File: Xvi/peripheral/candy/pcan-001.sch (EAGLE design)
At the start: 21 parts

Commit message: Optocoupler.
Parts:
- added JP1: Optorelay, pinhead:PINHD-1X2
- added OK1: LTV816, optocoupler:LTV816
- added R1: 220, rcl:R-EU_0204/5
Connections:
- new net N$17: OK1.A, R1.2
- new net N$19: JP1.2, OK1.EMIT
- new net N$20: JP1.1, OK1.COL
- net GND: now also OK1.C
- net MNTR: now also R1.1
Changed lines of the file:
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@@
 <part name="RN1" library="resistor-dil" library_urn="urn:adsk.eagle:library:342" deviceset="8R-N" device="" package3d_urn="urn:adsk.eagle:package:922/2" value="330"/>
 <part name="RN2" library="resistor-dil" library_urn="urn:adsk.eagle:library:342" deviceset="8R-N" device="" package3d_urn="urn:adsk.eagle:package:922/2" value="330"/>
+<part name="OK1" library="optocoupler" library_urn="urn:adsk.eagle:library:320" deviceset="LTV816" device="" package3d_urn="urn:adsk.eagle:package:21938/1"/>
+<part name="R1" library="rcl" library_urn="urn:adsk.eagle:library:334" deviceset="R-EU_" device="0204/5" package3d_urn="urn:adsk.eagle:package:23488/1" value="220"/>
+<part name="SUPPLY2" library="supply2" library_urn="urn:adsk.eagle:library:372" deviceset="GND" device=""/>
+<part name="JP1" library="pinhead" library_urn="urn:adsk.eagle:library:325" deviceset="PINHD-1X2" device="" package3d_urn="urn:adsk.eagle:package:22435/2" value="Optorelay"/>
 </parts>
 <sheets>
@@
 <attribute name="VALUE" x="55.88" y="17.272" size="1.778" layer="96"/>
 <attribute name="NAME" x="48.26" y="17.272" size="1.778" layer="95"/>
+</instance>
+<instance part="OK1" gate="G$1" x="121.92" y="226.06" smashed="yes">
+<attribute name="NAME" x="114.935" y="231.775" size="1.778" layer="95"/>
+<attribute name="VALUE" x="114.935" y="218.44" size="1.778" layer="96"/>
+</instance>
+<instance part="R1" gate="G$1" x="104.14" y="228.6" smashed="yes">
+<attribute name="NAME" x="100.33" y="230.0986" size="1.778" layer="95"/>
+<attribute name="VALUE" x="100.33" y="225.298" size="1.778" layer="96"/>
+</instance>
+<instance part="SUPPLY2" gate="GND" x="109.22" y="218.44" smashed="yes">
+<attribute name="VALUE" x="107.315" y="215.265" size="1.778" layer="96"/>
+</instance>
+<instance part="JP1" gate="G$1" x="144.78" y="223.52" smashed="yes">
+<attribute name="NAME" x="138.43" y="229.235" size="1.778" layer="95"/>
+<attribute name="VALUE" x="138.43" y="218.44" size="1.778" layer="96"/>
 </instance>
 </instances>
@@
 <label x="231.14" y="193.04" size="0.8128" layer="95" xref="yes"/>
 </segment>
+<segment>
+<pinref part="R1" gate="G$1" pin="1"/>
+<wire x1="99.06" y1="228.6" x2="96.52" y2="228.6" width="0.1524" layer="91"/>
+<label x="96.52" y="228.6" size="0.8128" layer="95" rot="R180" xref="yes"/>
+</segment>
 </net>
 <net name="GND" class="1">
@@
 <wire x1="200.66" y1="193.04" x2="200.66" y2="190.5" width="0.1524" layer="91"/>
 <pinref part="SUPPLY1" gate="GND" pin="GND"/>
+</segment>
+<segment>
+<pinref part="OK1" gate="G$1" pin="C"/>
+<wire x1="111.76" y1="223.52" x2="109.22" y2="223.52" width="0.1524" layer="91"/>
+<wire x1="109.22" y1="223.52" x2="109.22" y2="220.98" width="0.1524" layer="91"/>
+<pinref part="SUPPLY2" gate="GND" pin="GND"/>
+</segment>
+</net>
+<net name="N$17" class="0">
+<segment>
+<pinref part="OK1" gate="G$1" pin="A"/>
+<wire x1="111.76" y1="228.6" x2="109.22" y2="228.6" width="0.1524" layer="91"/>
+<pinref part="R1" gate="G$1" pin="2"/>
+</segment>
+</net>
+<net name="N$19" class="0">
+<segment>
+<pinref part="OK1" gate="G$1" pin="EMIT"/>
+<pinref part="JP1" gate="G$1" pin="2"/>
+<wire x1="129.54" y1="223.52" x2="142.24" y2="223.52" width="0.1524" layer="91"/>
+</segment>
+</net>
+<net name="N$20" class="0">
+<segment>
+<pinref part="OK1" gate="G$1" pin="COL"/>
+<wire x1="129.54" y1="228.6" x2="132.08" y2="228.6" width="0.1524" layer="91"/>
+<wire x1="132.08" y1="228.6" x2="132.08" y2="226.06" width="0.1524" layer="91"/>
+<pinref part="JP1" gate="G$1" pin="1"/>
+<wire x1="132.08" y1="226.06" x2="142.24" y2="226.06" width="0.1524" layer="91"/>
 </segment>
 </net>
@@
 packages will not be understood (or retained) with this version.
 </note>
+<note version="8.4" severity="warning">
+Since Version 8.4, EAGLE supports properties for SPICE simulation.
+Probes in schematics and SPICE mapping objects found in parts and library devices
+will not be understood with this version. Update EAGLE to the latest version
+for full support of SPICE simulation.
+</note>
 </compatibility>

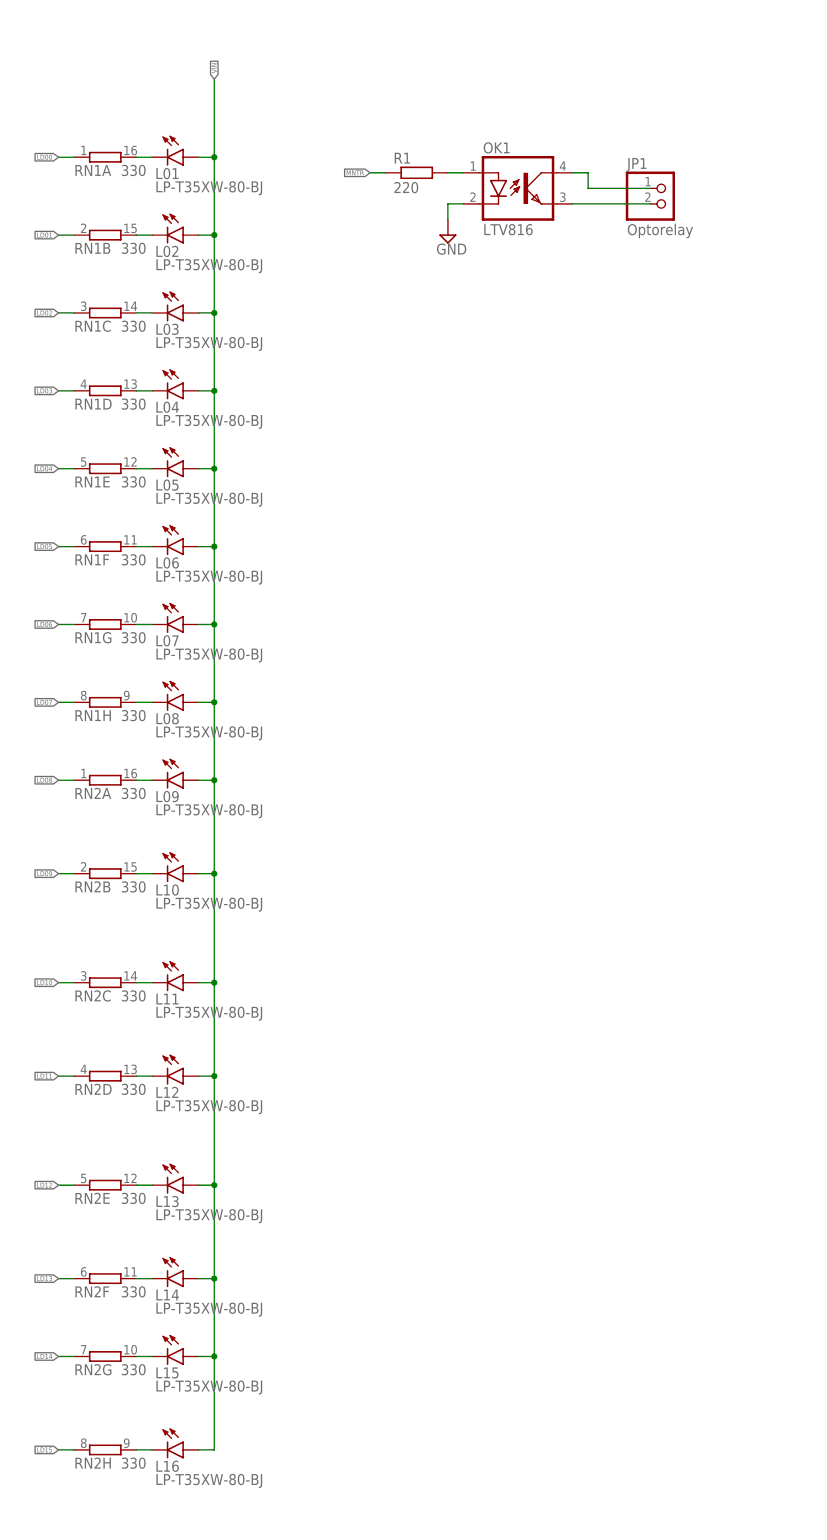
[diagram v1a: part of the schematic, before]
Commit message: Dual LEDs.
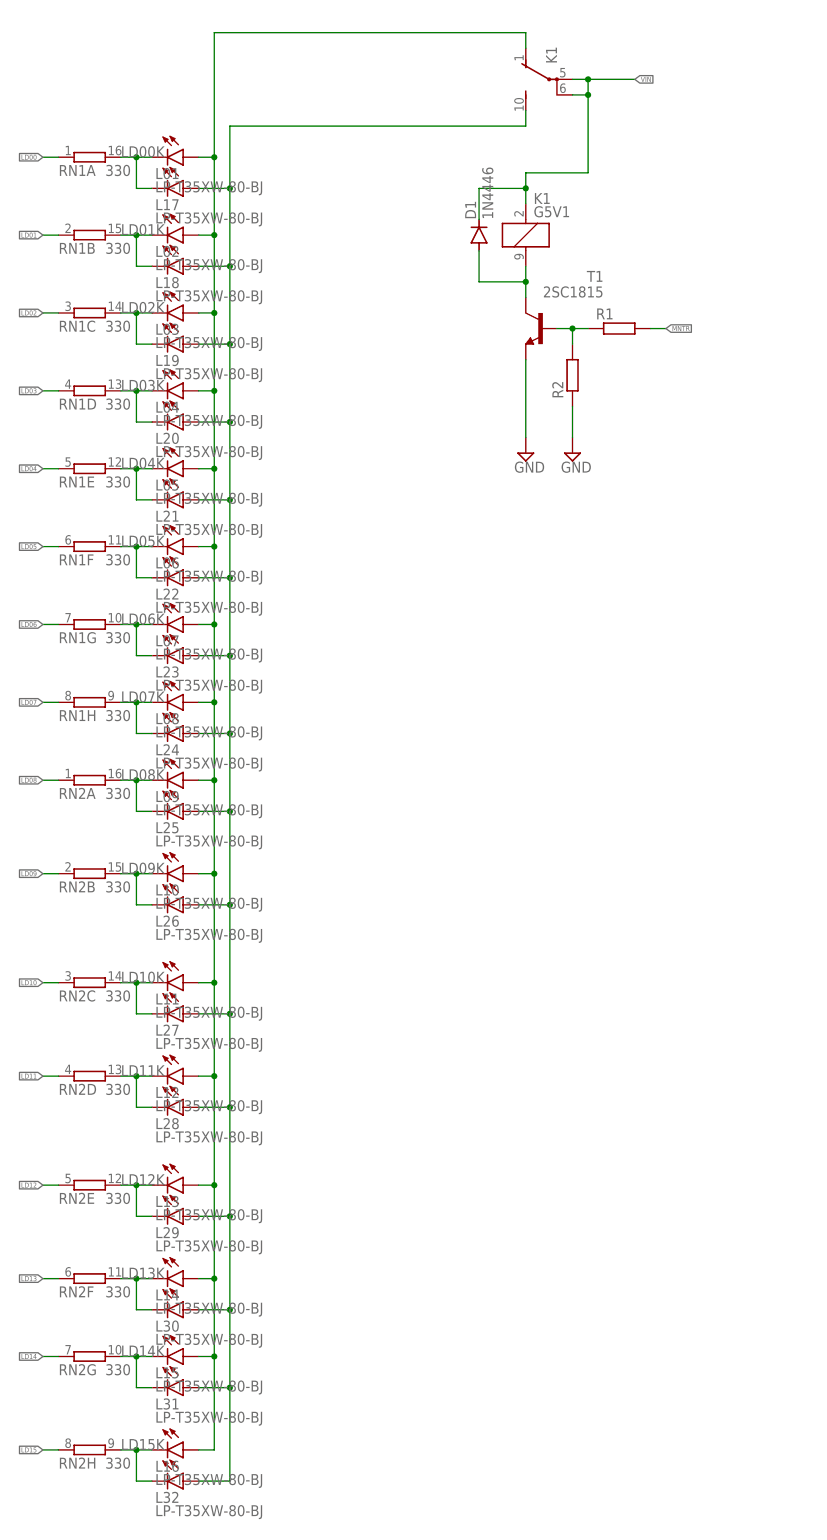
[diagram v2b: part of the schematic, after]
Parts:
- removed JP1: Optorelay, pinhead:PINHD-1X2
- removed OK1: LTV816, optocoupler:LTV816
- added D1: 1N4446, diode:1N4446
- added K1: G5V1, relay:G5V1
- added L17, L18, L19, L20, L21, L22, L23, L24, L25, L26, L27, L28, L29, L30, L31, L32: LP-T35XW-80-BJ, led:LEDKA-3528ASYC
- added R2: (no value), rcl:R-EU_0204/5
- added T1: 2SC1815, transistor:2SC1815
- R1: value 220 -> (none)
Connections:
- removed net N$1: L01.C, RN1A.2
- removed net N$10: L10.C, RN2B.2
- removed net N$11: L11.C, RN2C.2
- removed net N$12: L12.C, RN2D.2
- removed net N$13: L13.C, RN2E.2
- removed net N$14: L14.C, RN2F.2
- removed net N$15: L15.C, RN2G.2
- removed net N$16: L16.C, RN2H.2
- removed net N$2: L02.C, RN1B.2
- removed net N$20: JP1.1, OK1.COL
- removed net N$3: L03.C, RN1C.2
- removed net N$4: L04.C, RN1D.2
- removed net N$5: L05.C, RN1E.2
- removed net N$6: L06.C, RN1F.2
- removed net N$7: L07.C, RN1G.2
- removed net N$8: L08.C, RN1H.2
- removed net N$9: L09.C, RN2A.2
- new net LD00K: L01.C, L17.C, RN1A.2
- new net LD01K: L02.C, L18.C, RN1B.2
- new net LD02K: L03.C, L19.C, RN1C.2
- new net LD03K: L04.C, L20.C, RN1D.2
- new net LD04K: L05.C, L21.C, RN1E.2
- new net LD05K: L06.C, L22.C, RN1F.2
- new net LD06K: L07.C, L23.C, RN1G.2
- new net LD07K: L08.C, L24.C, RN1H.2
- new net LD08K: L09.C, L25.C, RN2A.2
- new net LD09K: L10.C, L26.C, RN2B.2
- new net LD10K: L11.C, L27.C, RN2C.2
- new net LD11K: L12.C, L28.C, RN2D.2
- new net LD12K: L13.C, L29.C, RN2E.2
- new net LD13K: L14.C, L30.C, RN2F.2
- new net LD14K: L15.C, L31.C, RN2G.2
- new net LD15K: L16.C, L32.C, RN2H.2
- new net VINA: K12.O, L01.A, L02.A, L03.A, L04.A, L05.A, L06.A, L07.A, L08.A, L09.A, L10.A, L11.A, L12.A, L13.A, L14.A, L15.A, L16.A
- new net VINB: K12.S, L17.A, L18.A, L19.A, L20.A, L21.A, L22.A, L23.A, L24.A, L25.A, L26.A, L27.A, L28.A, L29.A, L30.A, L31.A, L32.A
- net GND: now also R2.1, T1.E; no longer OK1.C
- net MNTR: now also R1.2; no longer R1.1
- net N$17: now also D1.A, K11.2, T1.C; no longer OK1.A, R1.2
- net N$19: now also R1.1, R2.2, T1.B; no longer JP1.2, OK1.EMIT
- net VIN: now also D1.C, K11.1, K12.P, K12.P@1; no longer L01.A, L02.A, L03.A, L04.A, L05.A, L06.A, L07.A, L08.A, L09.A, L10.A, L11.A, L12.A, L13.A, L14.A, L15.A, L16.A
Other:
- moved on the sheet: R1, RN1A, RN1B, RN1C, RN1D, RN1E, RN1F, RN1G, RN1H, RN2A, RN2B, RN2C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
